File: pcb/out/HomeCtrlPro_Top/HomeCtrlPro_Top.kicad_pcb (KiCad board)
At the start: 2 copper layers, 231.4 x 81.6 mm, 82 parts, among them J1 B2B, J2 We 0-7, J3 We 8-15, J4 We 16-23, J5 We 24-31, J6 RS485, J7 CAN, J8 TFT, SW1 RST, SW2 BOOT, SW3 GORA, SW4 DOL, SW5 OK, SW6 WSTECZ, U1 ESP32-S3-WROOM-1, U2 MCP23017, U3 MCP23017, U4 MAX485, U5 TJA1051

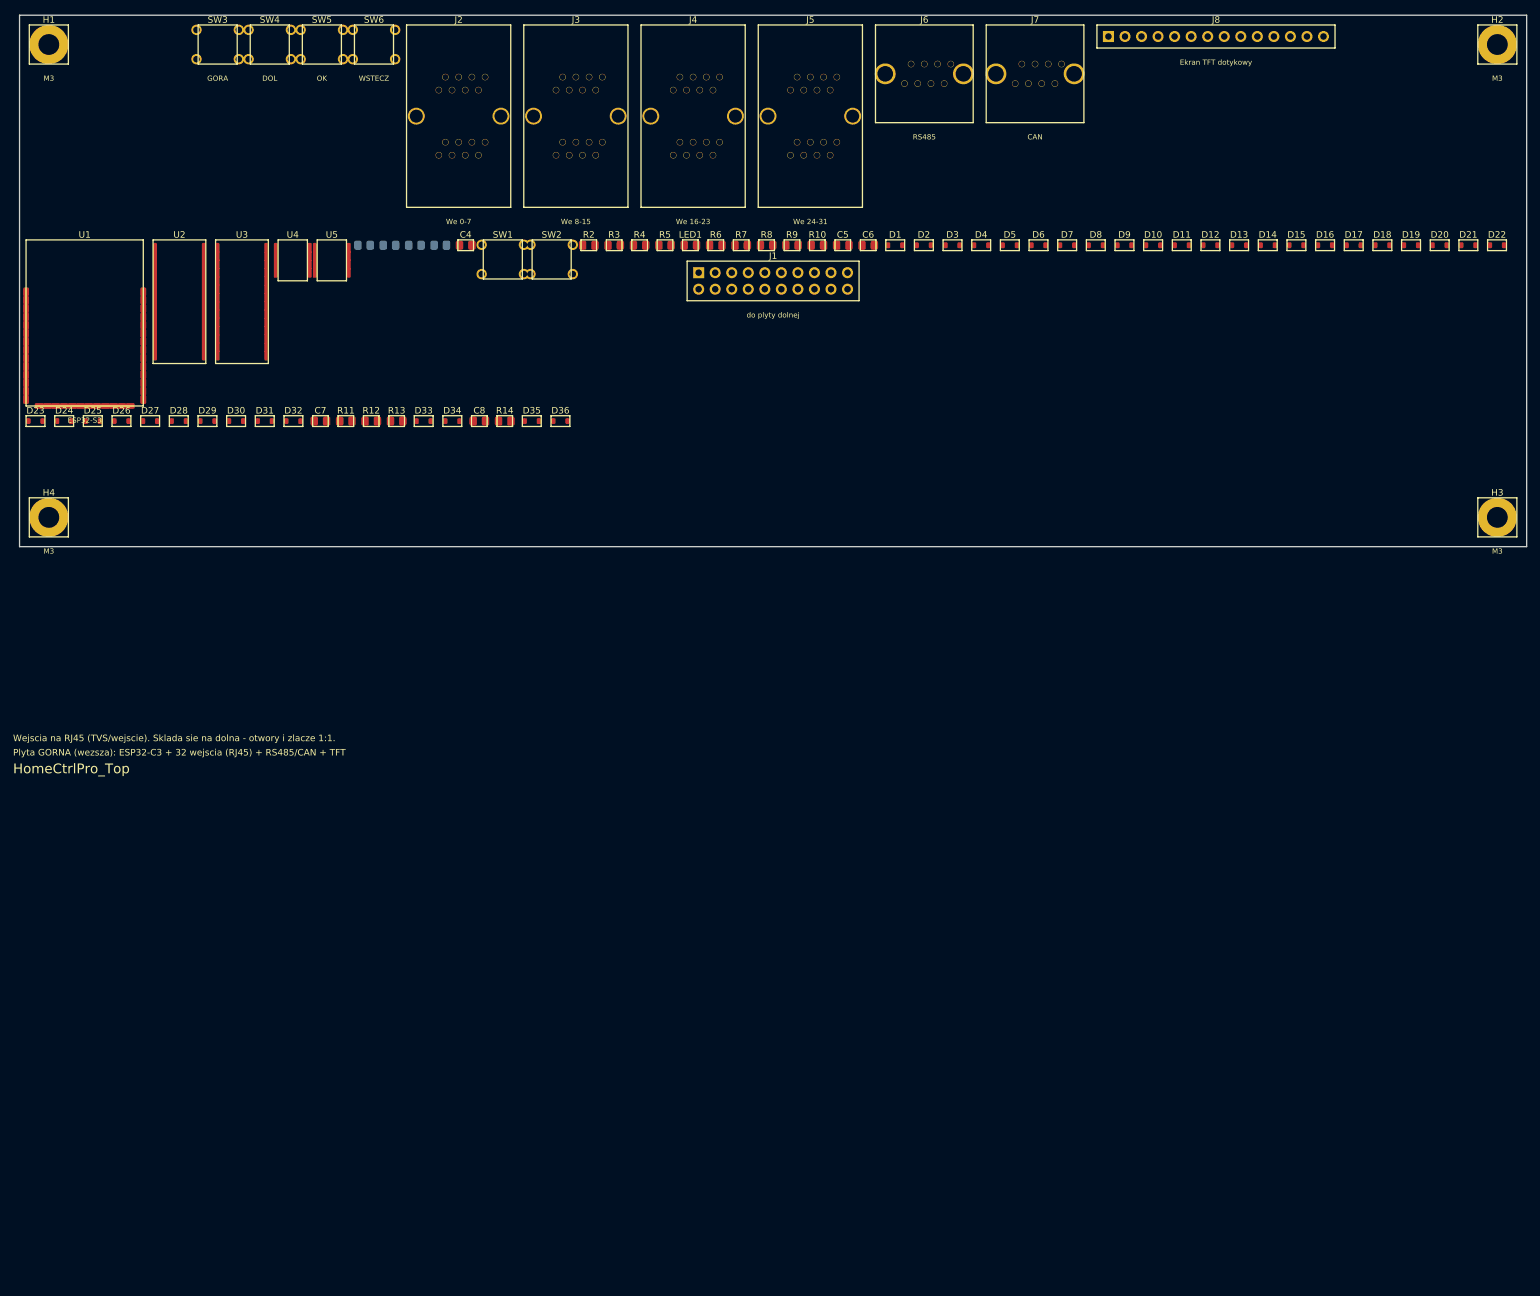
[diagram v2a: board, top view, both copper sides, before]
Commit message: Wiecej RJ45 (8 podwojnych=64 wej), zabezpieczenia, zlacza na obu krawedziach
- Wejscia: 8 podwojnych RJ45 = 16 portow = 64 wejscia (4 ekspandery MCP23017).
- Zabezpieczenia: PTC na kazde z 16 wyjsc, MOV na wyjsciach 230V, snubber RC na
  stykach przekaznikow, dlawik wspolny (CMC) + TVS na RS485/CAN, TVS na wyjsciach DC.
  Nowe czesci: PTC (polyfuse), CMC (common-mode choke).
- Layout: zlacza rozlozone na GORNA i DOLNA krawedz (_split_balanced) -> wezsza
  plytka; gestsze upakowanie, mniejszy luz wysokosci. auto_frame liczy szerokosc
  z rozlozenia na 2 krawedzie. HomeCtrlPro: 237 -> 155 mm szerokosci.

Oba PCB 0/0/0, testy 12/12, kiutils OK.

Co-Authored-By: Claude Opus 4.8 (1M context) <noreply@anthropic.com>
Claude-Session: https://claude.ai/code/session_01LNGxtK2Jv1rJLBLPTwFQ9C
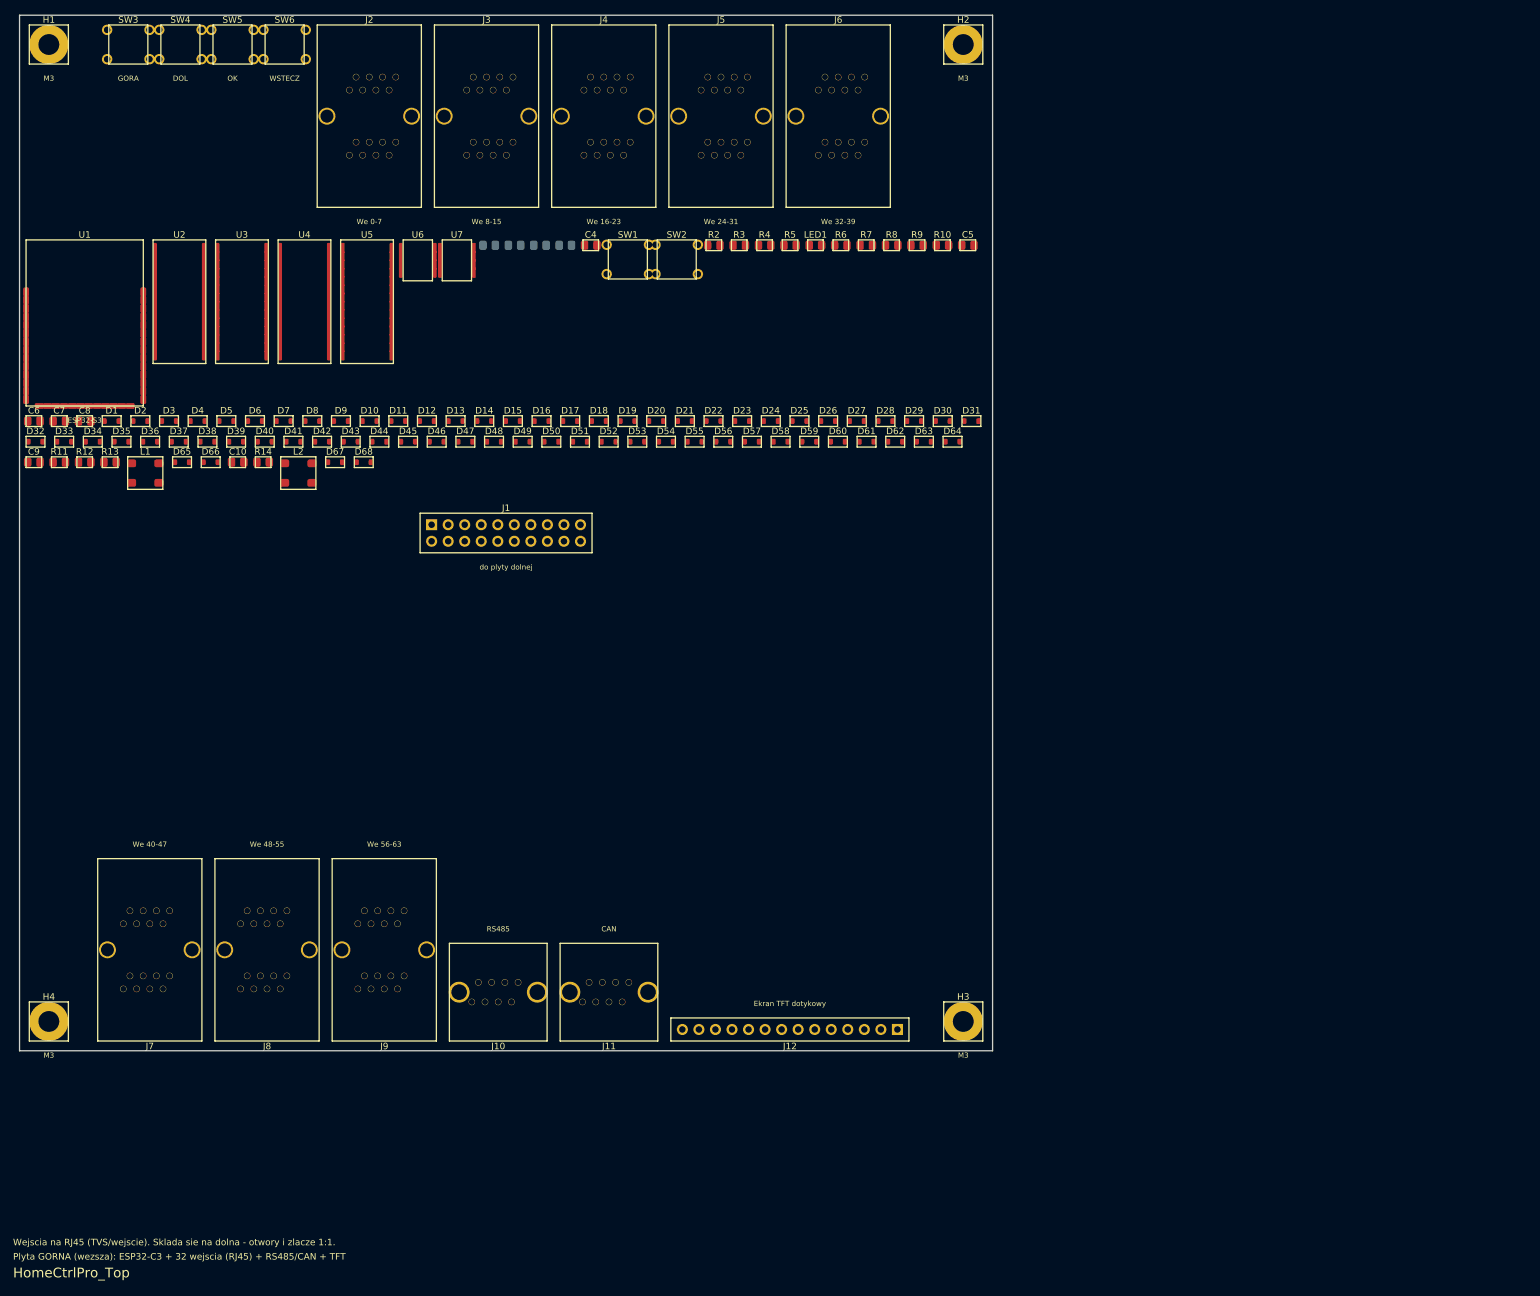
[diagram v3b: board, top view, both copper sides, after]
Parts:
- added C10: 100nF, pcbforge:C_0805, F.Cu at (36.5, 104.2)
- added C9: 100nF, pcbforge:C_0805, F.Cu at (5.20, 104.2)
- added D37: ESD, pcbforge:D_SOD-323, F.Cu at (27.4, 101.1)
- added D38: ESD, pcbforge:D_SOD-323, F.Cu at (31.9, 101.1)
- added D39: ESD, pcbforge:D_SOD-323, F.Cu at (36.2, 101.1)
- added D40: ESD, pcbforge:D_SOD-323, F.Cu at (40.6, 101.1)
- added D41: ESD, pcbforge:D_SOD-323, F.Cu at (45.0, 101.1)
- added D42: ESD, pcbforge:D_SOD-323, F.Cu at (49.5, 101.1)
- added D43: ESD, pcbforge:D_SOD-323, F.Cu at (53.9, 101.1)
- added D44: ESD, pcbforge:D_SOD-323, F.Cu at (58.2, 101.1)
- added D45: ESD, pcbforge:D_SOD-323, F.Cu at (62.6, 101.1)
- added D46: ESD, pcbforge:D_SOD-323, F.Cu at (67.0, 101.1)
- added D47: ESD, pcbforge:D_SOD-323, F.Cu at (71.5, 101.1)
- added D48: ESD, pcbforge:D_SOD-323, F.Cu at (75.8, 101.1)
- added D49: ESD, pcbforge:D_SOD-323, F.Cu at (80.2, 101.1)
- added D50: ESD, pcbforge:D_SOD-323, F.Cu at (84.7, 101.1)
- added D51: ESD, pcbforge:D_SOD-323, F.Cu at (89.0, 101.1)
- added D52: ESD, pcbforge:D_SOD-323, F.Cu at (93.5, 101.1)
- added D53: ESD, pcbforge:D_SOD-323, F.Cu at (97.8, 101.1)
- added D54: ESD, pcbforge:D_SOD-323, F.Cu at (102.2, 101.1)
- added D55: ESD, pcbforge:D_SOD-323, F.Cu at (106.7, 101.1)
- added D56: ESD, pcbforge:D_SOD-323, F.Cu at (111.0, 101.1)
- added D57: ESD, pcbforge:D_SOD-323, F.Cu at (115.5, 101.1)
- added D58: ESD, pcbforge:D_SOD-323, F.Cu at (119.8, 101.1)
- added D59: ESD, pcbforge:D_SOD-323, F.Cu at (124.2, 101.1)
- added D60: ESD, pcbforge:D_SOD-323, F.Cu at (128.7, 101.1)
- added D61: ESD, pcbforge:D_SOD-323, F.Cu at (133.1, 101.1)
- added D62: ESD, pcbforge:D_SOD-323, F.Cu at (137.4, 101.1)
- added D63: ESD, pcbforge:D_SOD-323, F.Cu at (141.8, 101.1)
- added D64: ESD, pcbforge:D_SOD-323, F.Cu at (146.2, 101.1)
- added D65: TVS, pcbforge:D_SOD-323, F.Cu at (27.9, 104.2)
- added D66: TVS, pcbforge:D_SOD-323, F.Cu at (32.4, 104.2)
- added D67: TVS, pcbforge:D_SOD-323, F.Cu at (51.5, 104.2)
- added D68: TVS, pcbforge:D_SOD-323, F.Cu at (55.9, 104.2)
- added J10: RS485, pcbforge:RJ45_8P8C, F.Cu at (76.5, 185.6)
- added J11: CAN, pcbforge:RJ45_8P8C, F.Cu at (93.5, 185.6)
- added J12: TFT, pcbforge:PinHeader_1x14_P2.54mm, F.Cu at (121.3, 191.3)
- added J9: We 56-63, pcbforge:RJ45_Dual, F.Cu at (59.0, 179.1)
- added L1: CMC, pcbforge:CMC_4, F.Cu at (22.3, 105.9)
- added L2: CMC, pcbforge:CMC_4, F.Cu at (45.8, 105.9)
- added U6: MAX485, pcbforge:SOIC-8, F.Cu at (64.2, 73.2)
- added U7: TJA1051, pcbforge:SOIC-8, F.Cu at (70.2, 73.2)
- D33, D34, D35, D36: value TVS -> ESD
- J6: value RS485 -> We 32-39; footprint pcbforge:RJ45_8P8C -> pcbforge:RJ45_Dual
- J7: value CAN -> We 40-47; footprint pcbforge:RJ45_8P8C -> pcbforge:RJ45_Dual
- J8: value TFT -> We 48-55; footprint pcbforge:PinHeader_1x14_P2.54mm -> pcbforge:RJ45_Dual
- U4: value MAX485 -> MCP23017; footprint pcbforge:SOIC-8 -> pcbforge:SOIC-28
- U5: value TJA1051 -> MCP23017; footprint pcbforge:SOIC-8 -> pcbforge:SOIC-28
- moved J8 202.2 mm to (41.0, 179.1), turned to 180 degrees
- moved J7 191.2 mm to (23.0, 179.1), turned to 180 degrees
- moved C6 130.9 mm to (5.20, 97.9)
- moved D10 123.3 mm to (56.8, 97.9)
- moved D14 123.3 mm to (74.3, 97.9)
- moved D15 123.3 mm to (78.8, 97.9)
- moved D19 123.3 mm to (96.3, 97.9)
- moved D20 123.3 mm to (100.8, 97.9)
- moved D4 123.3 mm to (30.4, 97.9)
- moved D5 123.3 mm to (34.8, 97.9)
- moved D9 123.3 mm to (52.4, 97.9)
- moved D12 123.3 mm to (65.5, 97.9)
- moved D13 123.3 mm to (70.0, 97.9)
- moved D17 123.3 mm to (87.5, 97.9)
- moved D18 123.3 mm to (92.0, 97.9)
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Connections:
- D33 pad 1: RS485_A -> IN32
- D34 pad 1: RS485_B -> IN33
- D35 pad 1: CAN_H -> IN34
- D36 pad 1: CAN_L -> IN35
- J6 pad 1: RS485_A -> 3V3
- J6 pad 2: RS485_B -> IN32
- J6 pad 3: GND -> IN33
- J6 pad 4: GND -> IN34
- J6 pad 5: GND -> IN35
- J6 pad 7: 3V3 -> GND
- J6 pad 8: 3V3 -> GND
- J7 pad 1: CAN_H -> 3V3
- J7 pad 2: CAN_L -> IN40
- J7 pad 3: GND -> IN41
- J7 pad 4: GND -> IN42
- J7 pad 5: GND -> IN43
- J7 pad 7: 3V3 -> GND
- J7 pad 8: 3V3 -> GND
- J8 pad 1: GND -> 3V3
- J8 pad 10: TOUCH_CS -> IN52
- J8 pad 11: TOUCH_IRQ -> IN53
- J8 pad 12: SPI_MISO -> IN54
- J8 pad 13: GND -> IN55
- J8 pad 14: 3V3 -> GND
- J8 pad 2: 3V3 -> IN48
- J8 pad 3: TFT_CS -> IN49
- J8 pad 4: TFT_RST -> IN50
- J8 pad 5: TFT_DC -> IN51
- J8 pad 6: SPI_MOSI -> GND
- J8 pad 7: SPI_SCK -> GND
- J8 pad 8: 3V3 -> GND
- J8 pad 9: SPI_MISO -> 3V3
- U4 pad 1: RS485_RXD -> IN40
- U4 pad 2: RS485_DE -> IN41
- U4 pad 3: RS485_DE -> IN42
- U4 pad 4: RS485_TXD -> IN43
- U4 pad 5: GND -> IN44
- U4 pad 6: RS485_A -> IN45
- U4 pad 7: RS485_B -> IN46
- U4 pad 8: 3V3 -> IN47
- U5 pad 1: CAN_TXD -> IN56
- U5 pad 2: GND -> IN57
- U5 pad 3: 3V3 -> IN58
- U5 pad 4: CAN_RXD -> IN59
- U5 pad 5: 3V3 -> IN60
- U5 pad 6: CAN_L -> IN61
- U5 pad 7: CAN_H -> IN62
- U5 pad 8: GND -> IN63
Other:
- board size 231.4 x 81.6 mm -> 149.4 x 159 mm
